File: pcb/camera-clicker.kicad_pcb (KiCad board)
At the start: 2 copper layers, 28 x 106.3 mm, 32 parts, among them J1 USB_C_Receptacle_USB2.0, J2 Conn_01x06, SW1 SW_SPST, SW2 BOOT, SW3 RST, SW4 SW_DPST_x2, U2 ESP32-MINI-1, U3 MCP2221AxST, U4 AZ1117-3.3

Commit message: fixing position
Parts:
- moved J1 5.63 mm to (141.0, 141.8)
- moved R7 5.60 mm to (151.0, 145.2)
- moved R8 5.60 mm to (136.9, 145.2)
- moved C7 5.58 mm to (146.3, 65.3)
- moved R1 5.58 mm to (139.4, 90.1)
- moved R10 5.58 mm to (151.8, 130.6)
- moved R11 5.58 mm to (142.8, 135.7)
- moved C6 5.58 mm to (146.3, 62.6)
- moved R6 5.58 mm to (136.8, 91.4)
- moved BT1 5.58 mm to (141.2, 86.6)
- moved C1 5.58 mm to (135.2, 87.3)
- moved C2 5.58 mm to (137.7, 87.3)
- moved C3 5.58 mm to (139.3, 118.8)
- moved C4 5.58 mm to (147.7, 118.8)
- moved D1 5.58 mm to (144.0, 96.3)
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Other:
- board size 28 x 106.3 mm -> 28 x 106 mm

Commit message: more pcb
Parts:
- added H1: MountingHole, MountingHole:MountingHole_2.2mm_M2, F.Cu at (156.0, 44.0)
- added H2: MountingHole, MountingHole:MountingHole_2.2mm_M2, F.Cu at (156.0, 146.0)
- added H3: MountingHole, MountingHole:MountingHole_2.2mm_M2, F.Cu at (132.0, 44.0)
- added H4: MountingHole, MountingHole:MountingHole_2.2mm_M2, F.Cu at (132.0, 146.0)
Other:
- outline, holes or cut-outs redrawn
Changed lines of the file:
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@@
     )
+  )
+  (footprint "MountingHole:MountingHole_2.2mm_M2" (layer "F.Cu")
+    (at 132 146)
+    (descr "Mounting Hole 2.2mm, no annular, M2")
+    (tags "mounting hole 2.2mm no annular m2")
+    (property "Sheetfile" "camera-clicker.kicad_sch")
+    (property "Sheetname" "")
+    (property "ki_description" "Mounting Hole without connection")
+    (property "ki_keywords" "mounting hole")
+    (attr exclude_from_pos_files)
+    (fp_text reference "H4" (at -8 -2) (layer "F.SilkS")
+        (effects (font (size 1 1) (thickness 0.15)))
+    )
+    (fp_text value "MountingHole" (at 0 3.2) (layer "F.Fab")
+        (effects (font (size 1 1) (thickness 0.15)))
+    )
+    (fp_text user "${REFERENCE}" (at 0 0) (layer "F.Fab")
+        (effects (font (size 1 1) (thickness 0.15)))
+    )
+    (fp_circle (center 0 0) (end 2.2 0)
+      (stroke (width 0.15) (type solid)) (fill none) (layer "Cmts.User"))
+    (fp_circle (center 0 0) (end 2.45 0)
+      (stroke (width 0.05) (type solid)) (fill none) (layer "F.CrtYd"))
+    (pad "" np_thru_hole circle (at 0 0) (size 2.2 2.2) (drill 2.2) (layers "*.Cu" "*.Mask"))
   )
   (footprint "Button_Switch_THT:SW_CuK_OS102011MA1QN1_SPDT_Angled" (layer "F.Cu")
@@
       (net 26 "/SW2") (pinfunction "B") (pintype "passive") (thermal_bridge_angle 45))
   )
+  (footprint "MountingHole:MountingHole_2.2mm_M2" (layer "F.Cu")
+    (at 156 44)
+    (descr "Mounting Hole 2.2mm, no annular, M2")
+    (tags "mounting hole 2.2mm no annular m2")
+    (property "Sheetfile" "camera-clicker.kicad_sch")
+    (property "Sheetname" "")
+    (property "ki_description" "Mounting Hole without connection")
+    (property "ki_keywords" "mounting hole")
+    (attr exclude_from_pos_files)
+    (fp_text reference "H1" (at 0 -3.2) (layer "F.SilkS")
+        (effects (font (size 1 1) (thickness 0.15)))
+    )
+    (fp_text value "MountingHole" (at 0 3.2) (layer "F.Fab")
+        (effects (font (size 1 1) (thickness 0.15)))
+    )
+    (fp_text user "${REFERENCE}" (at 0 0) (layer "F.Fab")
+        (effects (font (size 1 1) (thickness 0.15)))
+    )
+    (fp_circle (center 0 0) (end 2.2 0)
+      (stroke (width 0.15) (type solid)) (fill none) (layer "Cmts.User"))
+    (fp_circle (center 0 0) (end 2.45 0)
+      (stroke (width 0.05) (type solid)) (fill none) (layer "F.CrtYd"))
+    (pad "" np_thru_hole circle (at 0 0) (size 2.2 2.2) (drill 2.2) (layers "*.Cu" "*.Mask"))
+  )
   (footprint "Button_Switch_THT:SW_PUSH_6mm" (layer "F.Cu")
     (at 155 138.2 180)
@@
       (rotate (xyz 0 0 0))
     )
+  )
+  (footprint "MountingHole:MountingHole_2.2mm_M2" (layer "F.Cu")
+    (at 132 44)
+    (descr "Mounting Hole 2.2mm, no annular, M2")
+    (tags "mounting hole 2.2mm no annular m2")
+    (property "Sheetfile" "camera-clicker.kicad_sch")
+    (property "Sheetname" "")
+    (property "ki_description" "Mounting Hole without connection")
+    (property "ki_keywords" "mounting hole")
+    (attr exclude_from_pos_files)
+    (fp_text reference "H3" (at 0 -3.2) (layer "F.SilkS")
+        (effects (font (size 1 1) (thickness 0.15)))
+    )
+    (fp_text value "MountingHole" (at 0 3.2) (layer "F.Fab")
+        (effects (font (size 1 1) (thickness 0.15)))
+    )
+    (fp_text user "${REFERENCE}" (at 0 0) (layer "F.Fab")
+        (effects (font (size 1 1) (thickness 0.15)))
+    )
+    (fp_circle (center 0 0) (end 2.2 0)
+      (stroke (width 0.15) (type solid)) (fill none) (layer "Cmts.User"))
+    (fp_circle (center 0 0) (end 2.45 0)
+      (stroke (width 0.05) (type solid)) (fill none) (layer "F.CrtYd"))
+    (pad "" np_thru_hole circle (at 0 0) (size 2.2 2.2) (drill 2.2) (layers "*.Cu" "*.Mask"))
   )
   (footprint "Package_TO_SOT_SMD:SOT-89-3" (layer "F.Cu")
@@
       (rotate (xyz 0 0 0))
     )
+  )
+  (footprint "MountingHole:MountingHole_2.2mm_M2" (layer "F.Cu")
+    (at 156 146)
+    (descr "Mounting Hole 2.2mm, no annular, M2")
+    (tags "mounting hole 2.2mm no annular m2")
+    (property "Sheetfile" "camera-clicker.kicad_sch")
+    (property "Sheetname" "")
+    (property "ki_description" "Mounting Hole without connection")
+    (property "ki_keywords" "mounting hole")
+    (attr exclude_from_pos_files)
+    (fp_text reference "H2" (at 5 0) (layer "F.SilkS")
+        (effects (font (size 1 1) (thickness 0.15)))
+    )
+    (fp_text value "MountingHole" (at 0 3.2) (layer "F.Fab")
+        (effects (font (size 1 1) (thickness 0.15)))
+    )
+    (fp_text user "${REFERENCE}" (at 0 0) (layer "F.Fab")
+        (effects (font (size 1 1) (thickness 0.15)))
+    )
+    (fp_circle (center 0 0) (end 2.2 0)
+      (stroke (width 0.15) (type solid)) (fill none) (layer "Cmts.User"))
+    (fp_circle (center 0 0) (end 2.45 0)
+      (stroke (width 0.05) (type solid)) (fill none) (layer "F.CrtYd"))
+    (pad "" np_thru_hole circle (at 0 0) (size 2.2 2.2) (drill 2.2) (layers "*.Cu" "*.Mask"))
   )
   (footprint "Capacitor_SMD:C_1206_3216Metric" (layer "F.Cu")
@@
     )
   )
+  (gr_arc (start 130 44) (mid 130.585786 42.585786) (end 132 42)
+    (stroke (width 0.1) (type default)) (layer "Edge.Cuts"))
   (gr_rect (start 130 42) (end 158 148)
     (stroke (width 0.1) (type default)) (fill none) (layer "Edge.Cuts"))
+  (gr_arc (start 132 148) (mid 130.585786 147.414214) (end 130 146)
+    (stroke (width 0.1) (type default)) (layer "Edge.Cuts"))
+  (gr_arc (start 156 42) (mid 157.414214 42.585786) (end 158 44)
+    (stroke (width 0.1) (type default)) (layer "Edge.Cuts"))
+  (gr_arc (start 158 146) (mid 157.414214 147.414214) (end 156 148)
+    (stroke (width 0.1) (type default)) (layer "Edge.Cuts"))
   (gr_text "GND" (at 151.374762 98.4375) (layer "F.SilkS")
     (effects (font (size 1 1) (thickness 0.15)) (justify left bottom))

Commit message: more pcb
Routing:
- net +BATT: track 0.00 -> 120.6 mm, vias 0 -> 3
- net +5V: track 0.00 -> 96.3 mm, vias 0 -> 2
- net Net-(BT1-+): track 0.00 -> 90.0 mm, vias 0 -> 1
- net Net-(SW2-A): track 0.00 -> 82.7 mm
- net Net-(SW3-B): track 0.00 -> 80.1 mm
- net +3.3V: track 0.00 -> 54.9 mm, vias 0 -> 2
- net /RX: track 0.00 -> 44.7 mm, vias 0 -> 1
- net /TX: track 0.00 -> 40.9 mm, vias 0 -> 1
- net /D+: track 0.00 -> 38.9 mm, vias 0 -> 1
- net /D-: track 0.00 -> 37.4 mm
- net /SW2: track 0.00 -> 25.0 mm, vias 0 -> 2
- net /SW1: track 0.00 -> 23.8 mm
- net GND: track 0.00 -> 12.1 mm, vias 0 -> 4
- net Net-(D1-K): track 0.00 -> 8.69 mm
- net Net-(J1-CC2): track 0.00 -> 8.57 mm
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- added copper zone on B.Cu, net GND
- added copper zone on F.Cu, net GND
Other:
- outline, holes or cut-outs redrawn

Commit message: update pcb
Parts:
- removed C3: 22uf, Capacitor_SMD:C_1206_3216Metric
- removed C4: 10uf, Capacitor_SMD:C_1206_3216Metric
- removed C5: 0.47uf, Capacitor_SMD:C_1206_3216Metric
- removed R9: 10k, Resistor_SMD:R_1206_3216Metric
- removed U3: MCP2221AxST, Package_SO:TSSOP-14_4.4x5mm_P0.65mm
- removed U4: AZ1117-3.3, Package_TO_SOT_SMD:SOT-89-3
- U1: value ~ -> BQ25170
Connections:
- J1 pad A6: /D+ -> unconnected-(J1-D+-PadA6)
- J1 pad A7: /D- -> unconnected-(J1-D--PadA7)
- J1 pad B6: /D+ -> unconnected-(J1-D+-PadB6)
- J1 pad B7: /D- -> unconnected-(J1-D--PadB7)
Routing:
- net +3.3V: track 54.9 -> 0.00 mm, vias 2 -> 0
- net /D+: track 38.9 -> 0.00 mm, vias 1 -> 0
- net /D-: track 37.4 -> 0.00 mm
- net /RX: track 44.7 -> 24.5 mm, vias 1 -> 0
- net /TX: track 40.9 -> 27.4 mm, vias 1 -> 0
- net Net-(U3-~{RST}): track 5.74 -> 0.00 mm
- net GND: track 12.1 -> 17.7 mm, vias 4 -> 8
- net +5V: track 96.3 -> 90.8 mm

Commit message: new pcb design
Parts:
- removed J1: USB_C_Receptacle_USB2.0, Connector_USB:USB_C_Receptacle_GCT_USB4085
- added J3: USB_C_Receptacle_PowerOnly_6P, switch-footprints:USB_C_Receptacle_Amphenol_10164359-3A, F.Cu at (144.0, 134.6)
- SW2, SW3: footprint Button_Switch_THT:SW_PUSH_6mm -> switch-footprints:SW_SPST_PTS526
- moved SW2 33.6 mm to (144.0, 105.0)
- moved R11 31.7 mm to (138.2, 104.3), turned to 90 degrees
- moved SW3 27.5 mm to (144.0, 113.0)
- moved R10 22.7 mm to (138.3, 112.3), turned to -90 degrees
- moved R8 18.5 mm to (150.9, 133.2)
- moved R7 18.3 mm to (137.2, 133.1), turned to -90 degrees
- moved H2 11.0 mm to (156.0, 135.0)
- moved H4 11.0 mm to (132.0, 135.0)
- moved SW4 2.30 mm to (144.1, 55.0)
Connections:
- J2 pad 2: +3.3V -> +BATT
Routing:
- net Net-(SW2-A): track 82.7 -> 46.5 mm, vias 0 -> 2
- net Net-(SW3-B): track 80.1 -> 56.4 mm, vias 0 -> 2
- net +BATT: track 120.6 -> 104.1 mm, vias 3 -> 1
- net +5V: track 90.8 -> 77.1 mm, vias 2 -> 1
- net GND: track 17.7 -> 10.5 mm, vias 8 -> 7
- net /SW2: track 24.9 -> 27.2 mm
- net /SW1: track 23.8 -> 26.1 mm
- net Net-(J3-CC2): track 8.57 -> 7.78 mm
- net Net-(J3-CC1): track 7.31 -> 7.93 mm
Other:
- board size 28 x 106 mm -> 28 x 95 mm
- board text removed: "+3.3v"

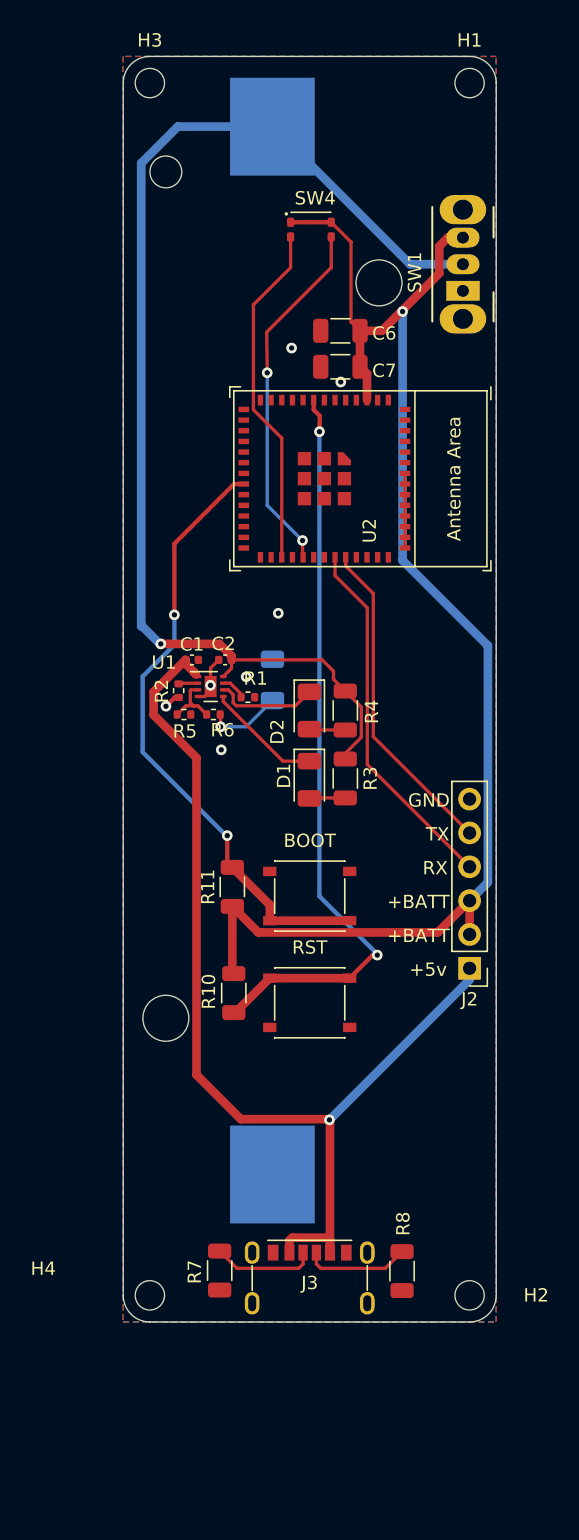
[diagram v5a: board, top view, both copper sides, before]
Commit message: updating pcb
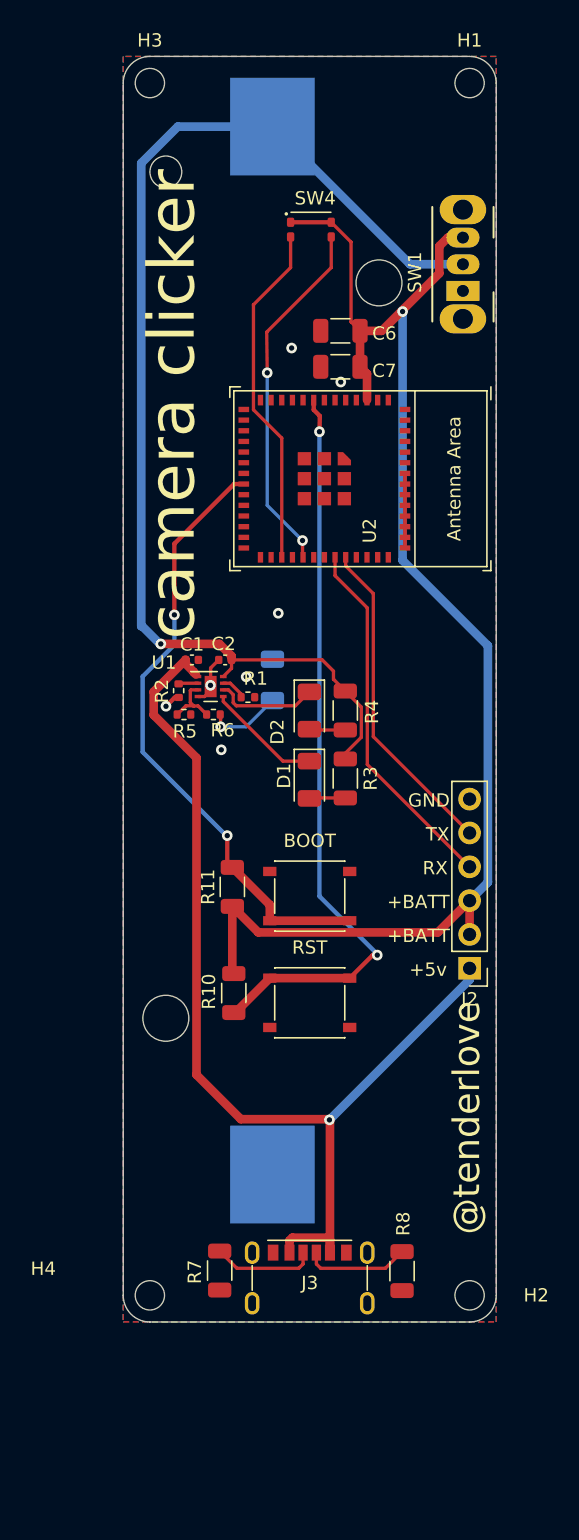
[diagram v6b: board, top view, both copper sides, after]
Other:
- board text added: "@tenderlove"
- board text added: "camera clicker"
- board text added: "github.com/tenderlove/camera-clicker"
